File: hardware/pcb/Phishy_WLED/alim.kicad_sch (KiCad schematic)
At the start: 17 parts, among them J1 Screw_Terminal_01x02, J2 Barrel_Jack_Switch, U1 LMR16006YQ, U3 LM7805MP

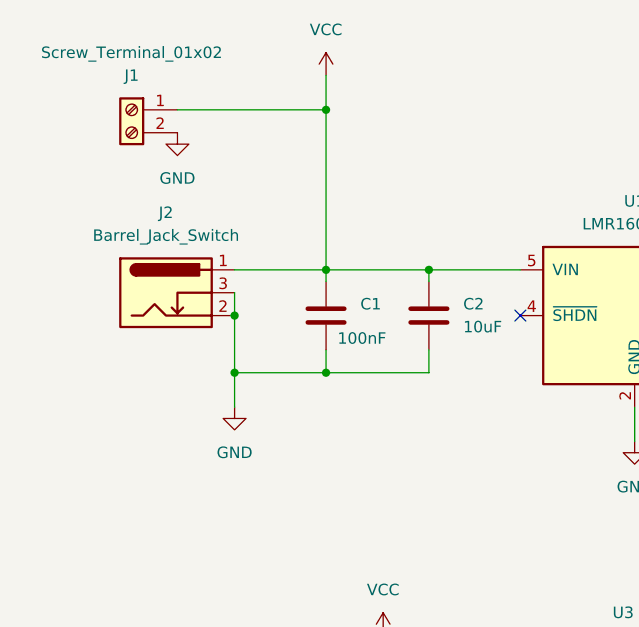
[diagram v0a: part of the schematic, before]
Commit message: footprints added !
all the footprints are here
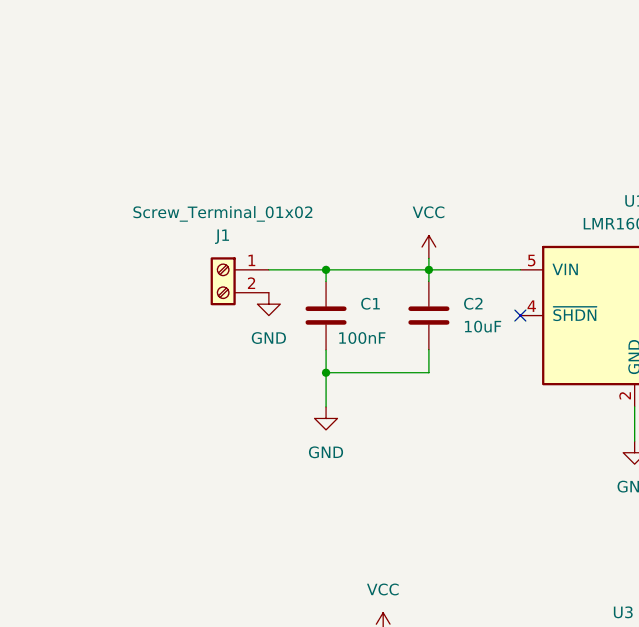
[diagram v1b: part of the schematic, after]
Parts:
- removed J2: Barrel_Jack_Switch, Connector_BarrelJack:BarrelJack_Horizontal, symbol Connector:Barrel_Jack_Switch
- D1: footprint (none) -> Diode_SMD:D_SMA
- L1: footprint (none) -> KiCad:INDPM120120X800N
- R1, R2: footprint (none) -> Resistor_SMD:R_0603_1608Metric
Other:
- moved on the sheet: J1
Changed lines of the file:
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@@
 (kicad_sch (version 20230121) (generator eeschema)
   (paper "A4")
-  (junction (at 48.26 74.93) (diameter 0) (color 0 0 0 0)
-  )
   (junction (at 91.44 118.11) (diameter 0) (color 0 0 0 0)
   )
@@
   (junction (at 58.42 63.5) (diameter 0) (color 0 0 0 0)
   )
-  (junction (at 48.26 68.58) (diameter 0) (color 0 0 0 0)
-  )
   (junction (at 113.03 107.95) (diameter 0) (color 0 0 0 0)
-  )
-  (junction (at 58.42 45.72) (diameter 0) (color 0 0 0 0)
   )
   (junction (at 149.86 68.58) (diameter 0) (color 0 0 0 0)
@@
     (stroke (width 0) (type default))
   )
-  (wire (pts (xy 69.85 74.93) (xy 58.42 74.93))
-    (stroke (width 0) (type default))
-  )
   (wire (pts (xy 101.6 116.84) (xy 101.6 118.11))
     (stroke (width 0) (type default))
@@
     (stroke (width 0) (type default))
   )
-  (wire (pts (xy 58.42 41.91) (xy 58.42 45.72))
-    (stroke (width 0) (type default))
-  )
   (wire (pts (xy 58.42 72.39) (xy 58.42 74.93))
     (stroke (width 0) (type default))
   )
-  (wire (pts (xy 58.42 45.72) (xy 58.42 63.5))
-    (stroke (width 0) (type default))
-  )
   (wire (pts (xy 99.06 107.95) (xy 101.6 107.95))
     (stroke (width 0) (type default))
@@
     (stroke (width 0) (type default))
   )
-  (wire (pts (xy 48.26 74.93) (xy 58.42 74.93))
+  (wire (pts (xy 58.42 74.93) (xy 69.85 74.93))
     (stroke (width 0) (type default))
   )
@@
     (stroke (width 0) (type default))
   )
-  (wire (pts (xy 41.91 45.72) (xy 58.42 45.72))
+  (wire (pts (xy 52.07 63.5) (xy 58.42 63.5))
     (stroke (width 0) (type default))
   )
@@
     (stroke (width 0) (type default))
   )
-  (wire (pts (xy 48.26 68.58) (xy 48.26 74.93))
+  (wire (pts (xy 69.85 62.23) (xy 69.85 63.5))
     (stroke (width 0) (type default))
   )
@@
     (stroke (width 0) (type default))
   )
-  (wire (pts (xy 48.26 63.5) (xy 58.42 63.5))
-    (stroke (width 0) (type default))
-  )
   (wire (pts (xy 135.89 68.58) (xy 140.97 68.58))
     (stroke (width 0) (type default))
@@
     (stroke (width 0) (type default))
   )
-  (wire (pts (xy 48.26 74.93) (xy 48.26 78.74))
-    (stroke (width 0) (type default))
-  )
-  (wire (pts (xy 48.26 66.04) (xy 48.26 68.58))
+  (wire (pts (xy 58.42 74.93) (xy 58.42 78.74))
     (stroke (width 0) (type default))
   )
@@
     )
   )
-  (symbol (lib_id "power:GND") (at 41.91 48.26 0) (unit 1)
-    (in_bom yes) (on_board yes) (dnp no) (fields_autoplaced)
-    (property "Reference" "#PWR01" (at 41.91 54.61 0)
-      (effects (font (size 1.27 1.27)) hide)
-    )
-    (property "Value" "GND" (at 41.91 53.34 0)
-      (effects (font (size 1.27 1.27)))
-    )
-    (property "Footprint" "" (at 41.91 48.26 0)
-      (effects (font (size 1.27 1.27)) hide)
-    )
-    (property "Datasheet" "" (at 41.91 48.26 0)
+  (symbol (lib_id "power:GND") (at 52.07 66.04 0) (unit 1)
+    (in_bom yes) (on_board yes) (dnp no) (fields_autoplaced)
+    (property "Reference" "#PWR01" (at 52.07 72.39 0)
+      (effects (font (size 1.27 1.27)) hide)
+    )
+    (property "Value" "GND" (at 52.07 71.12 0)
+      (effects (font (size 1.27 1.27)))
+    )
+    (property "Footprint" "" (at 52.07 66.04 0)
+      (effects (font (size 1.27 1.27)) hide)
+    )
+    (property "Datasheet" "" (at 52.07 66.04 0)
       (effects (font (size 1.27 1.27)) hide)
     )
@@
     )
   )
-  (symbol (lib_id "power:VCC") (at 58.42 41.91 0) (unit 1)
-    (in_bom yes) (on_board yes) (dnp no) (fields_autoplaced)
-    (property "Reference" "#PWR03" (at 58.42 45.72 0)
-      (effects (font (size 1.27 1.27)) hide)
-    )
-    (property "Value" "VCC" (at 58.42 36.83 0)
-      (effects (font (size 1.27 1.27)))
-    )
-    (property "Footprint" "" (at 58.42 41.91 0)
-      (effects (font (size 1.27 1.27)) hide)
-    )
-    (property "Datasheet" "" (at 58.42 41.91 0)
+  (symbol (lib_id "power:VCC") (at 69.85 62.23 0) (unit 1)
+    (in_bom yes) (on_board yes) (dnp no) (fields_autoplaced)
+    (property "Reference" "#PWR03" (at 69.85 66.04 0)
+      (effects (font (size 1.27 1.27)) hide)
+    )
+    (property "Value" "VCC" (at 69.85 57.15 0)
+      (effects (font (size 1.27 1.27)))
+    )
+    (property "Footprint" "" (at 69.85 62.23 0)
+      (effects (font (size 1.27 1.27)) hide)
+    )
+    (property "Datasheet" "" (at 69.85 62.23 0)
       (effects (font (size 1.27 1.27)) hide)
     )
@@
       (effects (font (size 1.27 1.27)) (justify left))
     )
-    (property "Footprint" "" (at 139.192 80.01 90)
+    (property "Footprint" "Resistor_SMD:R_0603_1608Metric" (at 139.192 80.01 90)
       (effects (font (size 1.27 1.27)) hide)
     )
@@
         (path "/f2195740-2ea3-423f-a798-d68f81431a72/d61fb2d2-8bce-4480-85f9-a87e8adb6d52"
           (reference "R8") (unit 1)
-        )
-      )
-    )
-  )
-  (symbol (lib_id "Connector:Barrel_Jack_Switch") (at 40.64 66.04 0) (unit 1)
-    (in_bom yes) (on_board yes) (dnp no) (fields_autoplaced)
-    (property "Reference" "J2" (at 40.64 57.15 0)
-      (effects (font (size 1.27 1.27)))
-    )
-    (property "Value" "Barrel_Jack_Switch" (at 40.64 59.69 0)
-      (effects (font (size 1.27 1.27)))
-    )
-    (property "Footprint" "Connector_BarrelJack:BarrelJack_Horizontal" (at 41.91 67.056 0)
-      (effects (font (size 1.27 1.27)) hide)
-    )
-    (property "Datasheet" "~" (at 41.91 67.056 0)
-      (effects (font (size 1.27 1.27)) hide)
-    )
-    (pin "1")
-    (pin "2")
-    (pin "3")
-    (instances
-      (project "Phishy_WLED"
-        (path "/04065f65-9c82-4e78-8d42-4173227f9ac1/c8e7b792-79fd-47c4-a59a-4e013840cd1a"
-          (reference "J2") (unit 1)
-        )
-      )
-      (project "DeskWorkShelf"
-        (path "/f2195740-2ea3-423f-a798-d68f81431a72"
-          (reference "J2") (unit 1)
-        )
-        (path "/f2195740-2ea3-423f-a798-d68f81431a72/d61fb2d2-8bce-4480-85f9-a87e8adb6d52"
-          (reference "J2") (unit 1)
         )
       )
@@
       (effects (font (size 1.27 1.27)) (justify left))
     )
-    (property "Footprint" "" (at 120.65 73.66 0)
+    (property "Footprint" "Diode_SMD:D_SMA" (at 120.65 73.66 0)
       (effects (font (size 1.27 1.27)) hide)
     )
@@
       (effects (font (size 1.27 1.27)) (justify left))
     )
-    (property "Footprint" "" (at 139.192 90.17 90)
+    (property "Footprint" "Resistor_SMD:R_0603_1608Metric" (at 139.192 90.17 90)
       (effects (font (size 1.27 1.27)) hide)
     )
@@
     )
   )
-  (symbol (lib_id "power:GND") (at 48.26 78.74 0) (unit 1)
-    (in_bom yes) (on_board yes) (dnp no) (fields_autoplaced)
-    (property "Reference" "#PWR02" (at 48.26 85.09 0)
-      (effects (font (size 1.27 1.27)) hide)
-    )
-    (property "Value" "GND" (at 48.26 83.82 0)
-      (effects (font (size 1.27 1.27)))
-    )
-    (property "Footprint" "" (at 48.26 78.74 0)
-      (effects (font (size 1.27 1.27)) hide)
-    )
-    (property "Datasheet" "" (at 48.26 78.74 0)
+  (symbol (lib_id "power:GND") (at 58.42 78.74 0) (unit 1)
+    (in_bom yes) (on_board yes) (dnp no) (fields_autoplaced)
+    (property "Reference" "#PWR02" (at 58.42 85.09 0)
+      (effects (font (size 1.27 1.27)) hide)
+    )
+    (property "Value" "GND" (at 58.42 83.82 0)
+      (effects (font (size 1.27 1.27)))
+    )
+    (property "Footprint" "" (at 58.42 78.74 0)
+      (effects (font (size 1.27 1.27)) hide)
+    )
+    (property "Datasheet" "" (at 58.42 78.74 0)
       (effects (font (size 1.27 1.27)) hide)
     )
@@
     )
   )
-  (symbol (lib_id "Connector:Screw_Terminal_01x02") (at 36.83 45.72 0) (mirror y) (unit 1)
+  (symbol (lib_id "Connector:Screw_Terminal_01x02") (at 46.99 63.5 0) (mirror y) (unit 1)
     (in_bom yes) (on_board yes) (dnp no)
-    (property "Reference" "J1" (at 36.83 41.91 0)
-      (effects (font (size 1.27 1.27)))
-    )
-    (property "Value" "Screw_Terminal_01x02" (at 36.83 39.37 0)
-      (effects (font (size 1.27 1.27)))
-    )
-    (property "Footprint" "TerminalBlock:TerminalBlock_bornier-2_P5.08mm" (at 36.83 45.72 0)
-      (effects (font (size 1.27 1.27)) hide)
-    )
-    (property "Datasheet" "~" (at 36.83 45.72 0)
+    (property "Reference" "J1" (at 46.99 59.69 0)
+      (effects (font (size 1.27 1.27)))
+    )
+    (property "Value" "Screw_Terminal_01x02" (at 46.99 57.15 0)
+      (effects (font (size 1.27 1.27)))
+    )
+    (property "Footprint" "TerminalBlock:TerminalBlock_bornier-2_P5.08mm" (at 46.99 63.5 0)
+      (effects (font (size 1.27 1.27)) hide)
+    )
+    (property "Datasheet" "~" (at 46.99 63.5 0)
       (effects (font (size 1.27 1.27)) hide)
     )
@@
       (effects (font (size 1.27 1.27)))
     )
-    (property "Footprint" "" (at 132.08 68.58 0)
-      (effects (font (size 1.27 1.27)) hide)
-    )
+    (property "Footprint" "KiCad:INDPM120120X800N" (at 132.08 68.58 0)
+      (effects (font (size 1.27 1.27)) hide)
+    )
